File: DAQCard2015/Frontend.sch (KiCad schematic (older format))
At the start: 12 parts, among them U1 RJ45x8, U2 AD5628

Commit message: Various updates to DAQ board focusing on power system
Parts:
- P7: renamed from P?; footprint (none) -> extras:N3432-D302RB
- U2: footprint Housings_SSOP:TSSOP-16_4.4x5mm_Pitch0.65mm -> extras:TSSOP-16_4.4x5mm_Pitch0.65mm
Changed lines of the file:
@@
 F 0 "U2" H 20750 4250 60  0000 C CNN
 F 1 "AD5628" H 20250 5350 60  0000 C CNN
-F 2 "Housings_SSOP:TSSOP-16_4.4x5mm_Pitch0.65mm" H 20650 4950 60  0001 C CNN
+F 2 "extras:TSSOP-16_4.4x5mm_Pitch0.65mm" H 20650 4950 60  0001 C CNN
 F 3 "" H 20650 4950 60  0000 C CNN
 	1    20450 4800
@@
 	19750 4450 19900 4450
 Wire Wire Line
-	19750 4150 19750 4200
-Wire Wire Line
-	19750 4200 19750 4450
+	19750 4150 19750 4450
 Wire Wire Line
 	21000 4650 21500 4650
 Wire Wire Line
-	21500 5500 21500 5150
-Wire Wire Line
-	21500 5150 21500 4650
-Wire Wire Line
-	21500 4650 21500 4200
+	21500 5500 21500 4200
 Wire Wire Line
 	21500 4200 19750 4200
@@
 RNGDAC_CSB
 Wire Wire Line
-	19400 4650 19450 4650
-Wire Wire Line
-	19450 4650 19900 4650
+	19400 4650 19900 4650
 Text GLabel 19400 4650 0    60   Input ~ 0
 3V3dig
@@
 $EndComp
 Wire Wire Line
-	20300 5500 20400 5500
-Wire Wire Line
-	20400 5500 21500 5500
+	20300 5500 21500 5500
 Connection ~ 21500 5150
 $Comp
@@
 $EndComp
 Wire Wire Line
-	19800 5500 19900 5500
-Wire Wire Line
-	19900 5500 20000 5500
-Wire Wire Line
-	19900 5150 19900 5500
-Wire Wire Line
-	19900 5500 19900 5700
+	19800 5500 20000 5500
+Wire Wire Line
+	19900 5150 19900 5700
 Connection ~ 19900 5500
 Wire Wire Line
@@
 $EndComp
 Wire Wire Line
-	1250 4250 1450 4250
-Wire Wire Line
-	1450 4250 1750 4250
-Wire Wire Line
-	1750 4250 2000 4250
-Wire Wire Line
-	2000 4250 2400 4250
+	1250 4250 2400 4250
 Connection ~ 2000 4250
 Wire Wire Line
@@
 	1750 4250 1750 4200
 Wire Wire Line
-	1750 3800 1750 3850
-Wire Wire Line
-	1750 3850 1750 3900
+	1750 3800 1750 3900
 Wire Wire Line
 	2000 4250 2000 4200
@@
 	2000 3900 2000 3850
 Wire Wire Line
-	1750 3850 2000 3850
-Wire Wire Line
-	2000 3850 2400 3850
+	1750 3850 2400 3850
 Connection ~ 1750 3850
 Connection ~ 2000 3850
 Wire Wire Line
-	1250 3500 1450 3500
-Wire Wire Line
-	1450 3500 1750 3500
-Wire Wire Line
-	1750 3500 2400 3500
+	1250 3500 2400 3500
 Wire Wire Line
 	1450 3500 1450 3750
@@
 SDA
 Wire Wire Line
-	7700 11950 7950 11950
-Wire Wire Line
-	7950 11950 8250 11950
-Wire Wire Line
-	7700 12150 7950 12150
-Wire Wire Line
-	7950 12150 8250 12150
+	7700 11950 8250 11950
+Wire Wire Line
+	7700 12150 8250 12150
 Text Label 7700 12050 0    60   ~ 0
 SCL
@@
 SCL
 $Comp
-L CONN_02X20_Double P?
+L CONN_02X20_Double P7
 U 1 1 55F4BDE8
 P 7450 11200
-F 0 "P?" H 7950 12500 50  0000 C CNN
+F 0 "P7" H 7950 12500 50  0000 C CNN
 F 1 "CONN_02X20_Double" H 7950 12400 50  0000 C CNN
-F 2 "" H 7450 10250 60  0000 C CNN
+F 2 "extras:N3432-D302RB" H 7450 10250 60  0001 C CNN
 F 3 "" H 7450 10250 60  0000 C CNN
 	1    7450 11200
@@
 $EndComp
 Wire Wire Line
-	7950 11950 7950 12150
-Wire Wire Line
-	7950 12150 7950 12300
+	7950 11950 7950 12300
 Connection ~ 7950 11950
 Connection ~ 7950 12150
 Wire Wire Line
-	6900 12300 7950 12300
-Wire Wire Line
-	7950 12300 9000 12300
-Wire Wire Line
-	9000 12300 9000 12150
-Wire Wire Line
-	9000 12150 9000 11950
+	6900 12300 9000 12300
+Wire Wire Line
+	9000 12300 9000 11950
 Connection ~ 9000 12150
 Wire Wire Line
-	6900 11950 6900 12150
-Wire Wire Line
-	6900 12150 6900 12300
+	6900 11950 6900 12300
 Connection ~ 7950 12300
 Connection ~ 6900 12150

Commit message: Updates to DAQ Board focusing on the power system and flood fills for it
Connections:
- net GNDdig is gone; now on net GND: C4.2, R5.1, U2.1 (LDAC_N), U2.14 (GND), U2.9 (CLR_N)
- net ADC_CLK+: now also R3.1; no longer R3.2
- net ADC_CLK-: now also R3.2; no longer R3.1
- net 1ADC_Vref renamed ADC1_Vref
- net 2ADC_Vref renamed ADC2_Vref
- net 3ADC_Vref renamed ADC3_Vref
- net 4ADC_Vref renamed ADC4_Vref
- net 5ADC_Vref renamed ADC5_Vref
- net 6ADC_Vref renamed ADC6_Vref
- net 7ADC_Vref renamed ADC7_Vref
- net 8ADC_Vref renamed ADC8_Vref
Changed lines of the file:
@@
 $Descr A2 23386 16535
 encoding utf-8
-Sheet 2 13
+Sheet 5 13
 Title ""
 Date ""
@@
 F28 "Vocm" I T 4000 3250 60
 $EndSheet
-Text HLabel 5450 3250 1    60   Input ~ 0
-ADC_CLK+
-Text HLabel 5350 3250 1    60   Input ~ 0
-ADC_CLK-
 $Sheet
 S 14550 3250 3400 1050
@@
 Text HLabel 12650 4600 3    60   Output ~ 0
 3DCO+
-Text HLabel 4900 3250 1    60   Input ~ 0
-ADC_SCLK
-Text HLabel 5000 3250 1    60   Input ~ 0
-ADC_SDIO
-Text HLabel 5100 3250 1    60   Input ~ 0
-1ADC_CSB
 $Sheet
 S 7350 7050 3400 1050
@@
 Text HLabel 17600 4600 3    60   Output ~ 0
 4D-D
-Text HLabel 8700 3250 1    60   Input ~ 0
-2ADC_CSB
-Text HLabel 12300 3250 1    60   Input ~ 0
-3ADC_CSB
-Text HLabel 15900 3250 1    60   Input ~ 0
-4ADC_CSB
-Text HLabel 15900 7050 1    60   Input ~ 0
-5ADC_CSB
-Text HLabel 12300 7050 1    60   Input ~ 0
-6ADC_CSB
-Text HLabel 8700 7050 1    60   Input ~ 0
-7ADC_CSB
-Text HLabel 5100 7050 1    60   Input ~ 0
-8ADC_CSB
 $Comp
 L AD5628 U2
@@
 $EndComp
 Text GLabel 19750 4150 1    60   Input ~ 0
-GNDdig
+GND
 Wire Wire Line
 	19900 4550 19550 4550
@@
 	21500 4200 19750 4200
 Connection ~ 19750 4200
-Text HLabel 19550 4550 1    60   Input ~ 0
-RNGDAC_CSB
 Wire Wire Line
 	19400 4650 19900 4650
@@
 	4550 3250 4550 3100
 Text Label 4550 3100 2    60   ~ 0
-1ADC_Vref
+ADC1_Vref
 Wire Wire Line
 	8200 3250 8200 3100
 Text Label 8200 3100 2    60   ~ 0
-2ADC_Vref
+ADC2_Vref
 Wire Wire Line
 	11800 3250 11800 3100
 Text Label 11800 3100 2    60   ~ 0
-3ADC_Vref
+ADC3_Vref
 Wire Wire Line
 	15400 3250 15400 3100
 Text Label 15400 3100 2    60   ~ 0
-4ADC_Vref
+ADC4_Vref
 Wire Wire Line
 	15400 7050 15400 6900
 Text Label 15400 6900 2    60   ~ 0
-5ADC_Vref
+ADC5_Vref
 Wire Wire Line
 	11800 7050 11800 6900
 Text Label 11800 6900 2    60   ~ 0
-6ADC_Vref
+ADC6_Vref
 Wire Wire Line
 	8200 7050 8200 6900
 Text Label 8200 6900 2    60   ~ 0
-7ADC_Vref
+ADC7_Vref
 Wire Wire Line
 	4550 7050 4550 6900
 Text Label 4550 6900 2    60   ~ 0
-8ADC_Vref
+ADC8_Vref
 Text Label 19900 4850 2    60   ~ 0
-3ADC_Vref
+ADC3_Vref
 Text Label 19900 4750 2    60   ~ 0
-1ADC_Vref
+ADC1_Vref
 Text Label 21000 4750 0    60   ~ 0
-2ADC_Vref
+ADC2_Vref
 Text Label 21000 4850 0    60   ~ 0
-4ADC_Vref
+ADC4_Vref
 Text Label 21000 4950 0    60   ~ 0
-6ADC_Vref
+ADC6_Vref
 Text Label 21000 5050 0    60   ~ 0
-8ADC_Vref
+ADC8_Vref
 Text Label 19900 4950 2    60   ~ 0
-5ADC_Vref
+ADC5_Vref
 Text Label 19900 5050 2    60   ~ 0
-7ADC_Vref
+ADC7_Vref
 Wire Wire Line
 	21500 5150 21000 5150
@@
 F28 "Vocm" I T 7600 3250 60
 $EndSheet
-Text HLabel 8500 3250 1    60   Input ~ 0
-ADC_SCLK
-Text HLabel 12100 3250 1    60   Input ~ 0
-ADC_SCLK
-Text HLabel 15700 3250 1    60   Input ~ 0
-ADC_SCLK
-Text HLabel 15700 7050 1    60   Input ~ 0
-ADC_SCLK
-Text HLabel 12100 7050 1    60   Input ~ 0
-ADC_SCLK
-Text HLabel 8500 7050 1    60   Input ~ 0
-ADC_SCLK
-Text HLabel 4900 7050 1    60   Input ~ 0
-ADC_SCLK
-Text HLabel 8600 3250 1    60   Input ~ 0
-ADC_SDIO
-Text HLabel 12200 3250 1    60   Input ~ 0
-ADC_SDIO
-Text HLabel 15800 3250 1    60   Input ~ 0
-ADC_SDIO
 Text HLabel 21000 4550 2    60   Input ~ 0
 ADC_SDIO
 Text HLabel 21000 4450 2    60   Input ~ 0
 ADC_SCLK
-Text HLabel 15800 7050 1    60   Input ~ 0
-ADC_SDIO
-Text HLabel 12200 7050 1    60   Input ~ 0
-ADC_SDIO
-Text HLabel 8600 7050 1    60   Input ~ 0
-ADC_SDIO
-Text HLabel 5000 7050 1    60   Input ~ 0
-ADC_SDIO
-Text HLabel 9050 3250 1    60   Input ~ 0
-ADC_CLK+
-Text HLabel 8950 3250 1    60   Input ~ 0
-ADC_CLK-
-Text HLabel 12650 3250 1    60   Input ~ 0
-ADC_CLK+
-Text HLabel 12550 3250 1    60   Input ~ 0
-ADC_CLK-
-Text HLabel 16250 3250 1    60   Input ~ 0
-ADC_CLK+
-Text HLabel 16150 3250 1    60   Input ~ 0
-ADC_CLK-
-Text HLabel 16250 7050 1    60   Input ~ 0
-ADC_CLK+
-Text HLabel 16150 7050 1    60   Input ~ 0
-ADC_CLK-
-Text HLabel 12650 7050 1    60   Input ~ 0
-ADC_CLK+
-Text HLabel 12550 7050 1    60   Input ~ 0
-ADC_CLK-
-Text HLabel 9050 7050 1    60   Input ~ 0
-ADC_CLK+
-Text HLabel 8950 7050 1    60   Input ~ 0
-ADC_CLK-
-Text HLabel 5450 7050 1    60   Input ~ 0
-ADC_CLK+
-Text HLabel 5350 7050 1    60   Input ~ 0
-ADC_CLK-
-Text HLabel 3100 7700 1    60   Input ~ 0
-ADC_CLK-
-Text HLabel 3200 7700 1    60   Input ~ 0
-ADC_CLK+
 $Sheet
 S 3750 7050 3400 1050
@@
 Connection ~ 7950 12300
 Connection ~ 6900 12150
+Text GLabel 5450 3250 1    40   Input ~ 0
+ADC_CLK+
+Text GLabel 5350 3250 1    40   Input ~ 0
+ADC_CLK-
+Text GLabel 5100 3250 1    40   Input ~ 0
+ADC1_CSB
+Text GLabel 5000 3250 1    40   Input ~ 0
+SPI_SDIO
+Text GLabel 4900 3250 1    40   Input ~ 0
+SPI_SCLK
+Text GLabel 9050 3250 1    40   Input ~ 0
+ADC_CLK+
+Text GLabel 8950 3250 1    40   Input ~ 0
+ADC_CLK-
+Text GLabel 8700 3250 1    40   Input ~ 0
+ADC2_CSB
+Text GLabel 8600 3250 1    40   Input ~ 0
+SPI_SDIO
+Text GLabel 8500 3250 1    40   Input ~ 0
+SPI_SCLK
+Text GLabel 12650 3250 1    40   Input ~ 0
+ADC_CLK+
+Text GLabel 12550 3250 1    40   Input ~ 0
+ADC_CLK-
+Text GLabel 12300 3250 1    40   Input ~ 0
+ADC3_CSB
+Text GLabel 12200 3250 1    40   Input ~ 0
+SPI_SDIO
+Text GLabel 12100 3250 1    40   Input ~ 0
+SPI_SCLK
+Text GLabel 16250 3250 1    40   Input ~ 0
+ADC_CLK+
+Text GLabel 16150 3250 1    40   Input ~ 0
+ADC_CLK-
+Text GLabel 15900 3250 1    40   Input ~ 0
+ADC4_CSB
+Text GLabel 15800 3250 1    40   Input ~ 0
+SPI_SDIO
+Text GLabel 15700 3250 1    40   Input ~ 0
+SPI_SCLK
+Text GLabel 16250 7050 1    40   Input ~ 0
+ADC_CLK+
+Text GLabel 16150 7050 1    40   Input ~ 0
+ADC_CLK-
+Text GLabel 15900 7050 1    40   Input ~ 0
+ADC5_CSB
+Text GLabel 15800 7050 1    40   Input ~ 0
+SPI_SDIO
+Text GLabel 15700 7050 1    40   Input ~ 0
+SPI_SCLK
+Text GLabel 12650 7050 1    40   Input ~ 0
+ADC_CLK+
+Text GLabel 12550 7050 1    40   Input ~ 0
+ADC_CLK-
+Text GLabel 12300 7050 1    40   Input ~ 0
+ADC6_CSB
+Text GLabel 12200 7050 1    40   Input ~ 0
+SPI_SDIO
+Text GLabel 12100 7050 1    40   Input ~ 0
+SPI_SCLK
+Text GLabel 9050 7050 1    40   Input ~ 0
+ADC_CLK+
+Text GLabel 8950 7050 1    40   Input ~ 0
+ADC_CLK-
+Text GLabel 8700 7050 1    40   Input ~ 0
+ADC7_CSB
+Text GLabel 8600 7050 1    40   Input ~ 0
+SPI_SDIO
+Text GLabel 8500 7050 1    40   Input ~ 0
+SPI_SCLK
+Text GLabel 5450 7050 1    40   Input ~ 0
+ADC_CLK+
+Text GLabel 5350 7050 1    40   Input ~ 0
+ADC_CLK-
+Text GLabel 5100 7050 1    40   Input ~ 0
+ADC8_CSB
+Text GLabel 5000 7050 1    40   Input ~ 0
+SPI_SDIO
+Text GLabel 4900 7050 1    40   Input ~ 0
+SPI_SCLK
+Text GLabel 3100 7700 1    40   Input ~ 0
+ADC_CLK+
+Text GLabel 3200 7700 1    40   Input ~ 0
+ADC_CLK-
+Text GLabel 19550 4550 1    60   Input ~ 0
+RNGDAC_CSB
+Text GLabel 10250 10300 2    40   Input ~ 0
+Vana
+Text GLabel 10250 10400 2    40   Input ~ 0
+Vana
+Text GLabel 10250 10500 2    40   Input ~ 0
+Vana
+Text GLabel 10250 10600 2    40   Input ~ 0
+Vana
+Text GLabel 10250 10700 2    40   Input ~ 0
+Vana
+Text GLabel 10250 10800 2    40   Input ~ 0
+Vana
+Text GLabel 10250 10900 2    40   Input ~ 0
+Vana
+Text GLabel 10250 11000 2    40   Input ~ 0
+Vana
+Text GLabel 10250 11100 2    40   Input ~ 0
+Vana
+Text GLabel 10250 11200 2    40   Input ~ 0
+Vana
+Text GLabel 10250 11300 2    40   Input ~ 0
+Vana
+Text GLabel 10250 11400 2    40   Input ~ 0
+Vana
 $EndSCHEMATC

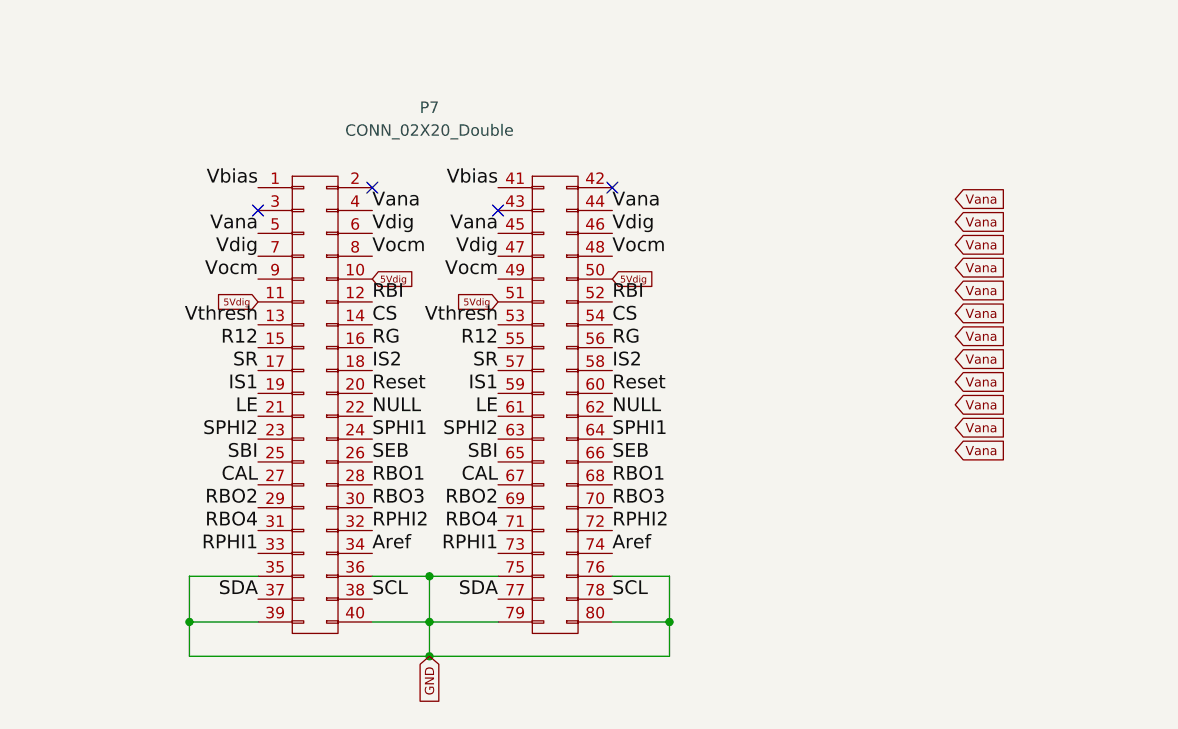
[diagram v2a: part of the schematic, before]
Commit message: Updates to DAQ board focusing on Support electronics
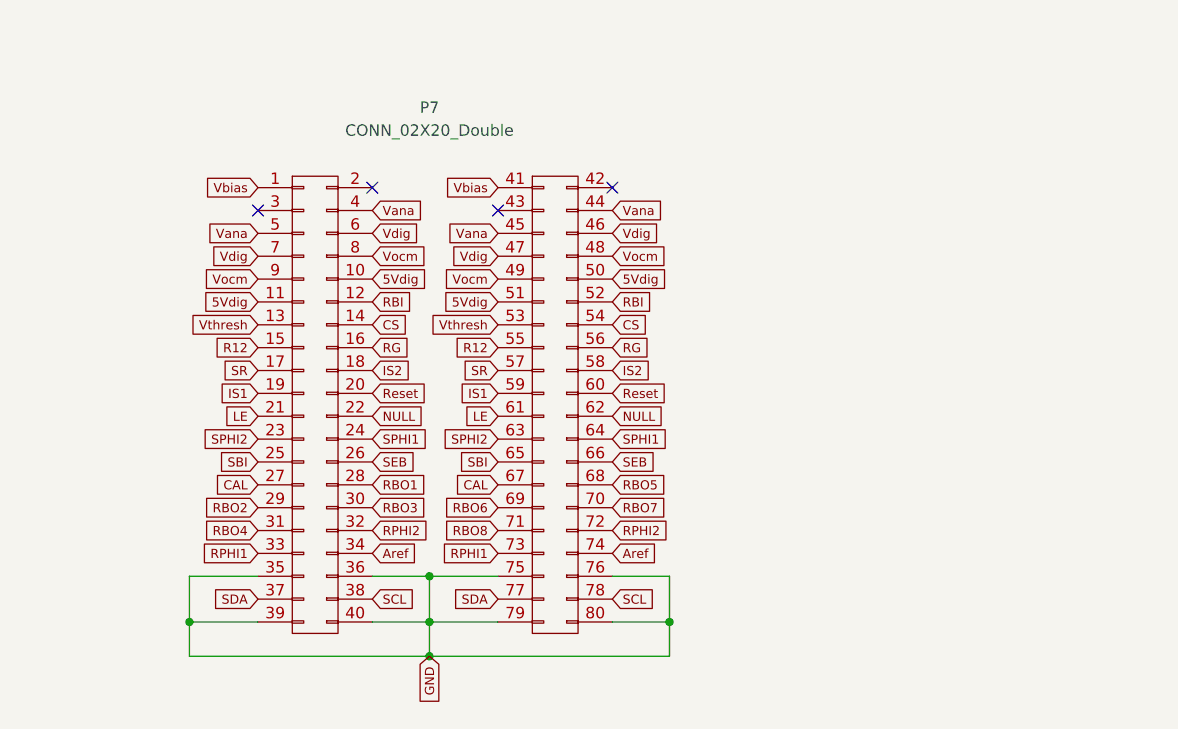
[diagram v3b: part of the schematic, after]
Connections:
- net RBO1: no longer P7.68 (P28)
- net RBO2: no longer P7.69 (P29)
- net RBO3: no longer P7.70 (P30)
- net RBO4: no longer P7.71 (P31)
- new net RBO5: P7.68 (P28)
- new net RBO6: P7.69 (P29)
- new net RBO7: P7.70 (P30)
- new net RBO8: P7.71 (P31)
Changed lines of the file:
@@
 Wire Wire Line
 	17350 2650 17350 2550
-Text Label 7200 10250 2    60   ~ 0
-Vbias
 NoConn ~ 7700 10250
 NoConn ~ 7200 10350
-Text Label 7700 10350 0    60   ~ 0
-Vana
-Text Label 7200 10450 2    60   ~ 0
-Vana
-Text Label 7700 10450 0    60   ~ 0
-Vdig
-Text Label 7200 10550 2    60   ~ 0
-Vdig
-Text Label 7700 10550 0    60   ~ 0
-Vocm
-Text Label 7200 10650 2    60   ~ 0
-Vocm
-Text GLabel 7700 10650 2    30   Input ~ 0
-5Vdig
-Text GLabel 7200 10750 0    30   Input ~ 0
-5Vdig
-Text Label 7700 10750 0    60   ~ 0
-RBI
-Wire Wire Line
-	7200 10750 7200 10750
-Wire Wire Line
-	7700 10650 7700 10650
-Text Label 7200 10850 2    60   ~ 0
-Vthresh
-Text Label 7700 10850 0    60   ~ 0
-CS
-Text Label 7200 10950 2    60   ~ 0
-R12
-Text Label 7700 10950 0    60   ~ 0
-RG
-Text Label 7200 11050 2    60   ~ 0
-SR
-Text Label 7700 11050 0    60   ~ 0
-IS2
-Text Label 7200 11150 2    60   ~ 0
-IS1
-Text Label 7700 11150 0    60   ~ 0
-Reset
-Text Label 7200 11250 2    60   ~ 0
-LE
-Text Label 7700 11250 0    60   ~ 0
-NULL
-Text Label 7200 11350 2    60   ~ 0
-SPHI2
-Text Label 7700 11350 0    60   ~ 0
-SPHI1
-Text Label 7200 11450 2    60   ~ 0
-SBI
-Text Label 7700 11450 0    60   ~ 0
-SEB
-Text Label 7200 11550 2    60   ~ 0
-CAL
-Text Label 7700 11550 0    60   ~ 0
-RBO1
-Text Label 7200 11650 2    60   ~ 0
-RBO2
-Text Label 7700 11650 0    60   ~ 0
-RBO3
-Text Label 7200 11750 2    60   ~ 0
-RBO4
-Text Label 7700 11750 0    60   ~ 0
-RPHI2
-Text Label 7200 11850 2    60   ~ 0
-RPHI1
-Text Label 7700 11850 0    60   ~ 0
-Aref
 Wire Wire Line
 	6900 11950 7200 11950
 Wire Wire Line
 	6900 12150 7200 12150
-Text Label 7200 12050 2    60   ~ 0
-SDA
 Wire Wire Line
 	7700 11950 8250 11950
 Wire Wire Line
 	7700 12150 8250 12150
-Text Label 7700 12050 0    60   ~ 0
-SCL
-Text Label 8250 10250 2    60   ~ 0
-Vbias
 NoConn ~ 8750 10250
 NoConn ~ 8250 10350
-Text Label 8750 10350 0    60   ~ 0
-Vana
-Text Label 8250 10450 2    60   ~ 0
-Vana
-Text Label 8750 10450 0    60   ~ 0
-Vdig
-Text Label 8250 10550 2    60   ~ 0
-Vdig
-Text Label 8750 10550 0    60   ~ 0
-Vocm
-Text Label 8250 10650 2    60   ~ 0
-Vocm
-Text GLabel 8750 10650 2    30   Input ~ 0
-5Vdig
-Text GLabel 8250 10750 0    30   Input ~ 0
-5Vdig
-Text Label 8750 10750 0    60   ~ 0
-RBI
-Wire Wire Line
-	8250 10750 8250 10750
-Wire Wire Line
-	8750 10650 8750 10650
-Text Label 8250 10850 2    60   ~ 0
-Vthresh
-Text Label 8750 10850 0    60   ~ 0
-CS
-Text Label 8250 10950 2    60   ~ 0
-R12
-Text Label 8750 10950 0    60   ~ 0
-RG
-Text Label 8250 11050 2    60   ~ 0
-SR
-Text Label 8750 11050 0    60   ~ 0
-IS2
-Text Label 8250 11150 2    60   ~ 0
-IS1
-Text Label 8750 11150 0    60   ~ 0
-Reset
-Text Label 8250 11250 2    60   ~ 0
-LE
-Text Label 8750 11250 0    60   ~ 0
-NULL
-Text Label 8250 11350 2    60   ~ 0
-SPHI2
-Text Label 8750 11350 0    60   ~ 0
-SPHI1
-Text Label 8250 11450 2    60   ~ 0
-SBI
-Text Label 8750 11450 0    60   ~ 0
-SEB
-Text Label 8250 11550 2    60   ~ 0
-CAL
-Text Label 8750 11550 0    60   ~ 0
-RBO1
-Text Label 8250 11650 2    60   ~ 0
-RBO2
-Text Label 8750 11650 0    60   ~ 0
-RBO3
-Text Label 8250 11750 2    60   ~ 0
-RBO4
-Text Label 8750 11750 0    60   ~ 0
-RPHI2
-Text Label 8250 11850 2    60   ~ 0
-RPHI1
-Text Label 8750 11850 0    60   ~ 0
-Aref
 Text GLabel 7950 12300 3    40   Input ~ 0
 GND
-Text Label 8250 12050 2    60   ~ 0
-SDA
 Wire Wire Line
 	8750 11950 9000 11950
 Wire Wire Line
 	8750 12150 9000 12150
-Text Label 8750 12050 0    60   ~ 0
-SCL
 $Comp
 L CONN_02X20_Double P7
@@
 Text GLabel 19550 4550 1    60   Input ~ 0
 RNGDAC_CSB
-Text GLabel 10250 10300 2    40   Input ~ 0
-Vana
-Text GLabel 10250 10400 2    40   Input ~ 0
-Vana
-Text GLabel 10250 10500 2    40   Input ~ 0
-Vana
-Text GLabel 10250 10600 2    40   Input ~ 0
-Vana
-Text GLabel 10250 10700 2    40   Input ~ 0
-Vana
-Text GLabel 10250 10800 2    40   Input ~ 0
-Vana
-Text GLabel 10250 10900 2    40   Input ~ 0
-Vana
-Text GLabel 10250 11000 2    40   Input ~ 0
-Vana
-Text GLabel 10250 11100 2    40   Input ~ 0
-Vana
-Text GLabel 10250 11200 2    40   Input ~ 0
-Vana
-Text GLabel 10250 11300 2    40   Input ~ 0
-Vana
-Text GLabel 10250 11400 2    40   Input ~ 0
-Vana
+Text GLabel 7700 10350 2    40   Input ~ 0
+Vana
+Text GLabel 7700 10450 2    40   Input ~ 0
+Vdig
+Text GLabel 7700 10550 2    40   Input ~ 0
+Vocm
+Text GLabel 7700 10750 2    40   Input ~ 0
+RBI
+Text GLabel 7700 10850 2    40   Input ~ 0
+CS
+Text GLabel 7700 10950 2    40   Input ~ 0
+RG
+Text GLabel 7700 11050 2    40   Input ~ 0
+IS2
+Text GLabel 7700 11150 2    40   Input ~ 0
+Reset
+Text GLabel 7700 11250 2    40   Input ~ 0
+NULL
+Text GLabel 7700 11350 2    40   Input ~ 0
+SPHI1
+Text GLabel 7700 11450 2    40   Input ~ 0
+SEB
+Text GLabel 7700 11550 2    40   Input ~ 0
+RBO1
+Text GLabel 7700 11650 2    40   Input ~ 0
+RBO3
+Text GLabel 7700 11750 2    40   Input ~ 0
+RPHI2
+Text GLabel 7700 11850 2    40   Input ~ 0
+Aref
+Text GLabel 7700 10650 2    40   Input ~ 0
+5Vdig
+Text GLabel 7200 11850 0    40   Input ~ 0
+RPHI1
+Text GLabel 7200 11750 0    40   Input ~ 0
+RBO4
+Text GLabel 7200 11650 0    40   Input ~ 0
+RBO2
+Text GLabel 7200 11450 0    40   Input ~ 0
+SBI
+Text GLabel 7200 11350 0    40   Input ~ 0
+SPHI2
+Text GLabel 7200 11250 0    40   Input ~ 0
+LE
+Text GLabel 7200 11150 0    40   Input ~ 0
+IS1
+Text GLabel 7200 11050 0    40   Input ~ 0
+SR
+Text GLabel 7200 10950 0    40   Input ~ 0
+R12
+Text GLabel 7200 10850 0    40   Input ~ 0
+Vthresh
+Text GLabel 7200 10750 0    40   Input ~ 0
+5Vdig
+Text GLabel 7200 10650 0    40   Input ~ 0
+Vocm
+Text GLabel 7200 10550 0    40   Input ~ 0
+Vdig
+Text GLabel 7200 10450 0    40   Input ~ 0
+Vana
+Text GLabel 7200 10250 0    40   Input ~ 0
+Vbias
+Text GLabel 7200 11550 0    40   Input ~ 0
+CAL
+Text GLabel 7200 12050 0    40   Input ~ 0
+SDA
+Text GLabel 7700 12050 2    40   Input ~ 0
+SCL
+Text GLabel 8250 11850 0    40   Input ~ 0
+RPHI1
+Text GLabel 8250 11750 0    40   Input ~ 0
+RBO8
+Text GLabel 8250 11650 0    40   Input ~ 0
+RBO6
+Text GLabel 8250 11450 0    40   Input ~ 0
+SBI
+Text GLabel 8250 11350 0    40   Input ~ 0
+SPHI2
+Text GLabel 8250 11250 0    40   Input ~ 0
+LE
+Text GLabel 8250 11150 0    40   Input ~ 0
+IS1
+Text GLabel 8250 11050 0    40   Input ~ 0
+SR
+Text GLabel 8250 10950 0    40   Input ~ 0
+R12
+Text GLabel 8250 10850 0    40   Input ~ 0
+Vthresh
+Text GLabel 8250 10750 0    40   Input ~ 0
+5Vdig
+Text GLabel 8250 10650 0    40   Input ~ 0
+Vocm
+Text GLabel 8250 10550 0    40   Input ~ 0
+Vdig
+Text GLabel 8250 10450 0    40   Input ~ 0
+Vana
+Text GLabel 8250 10250 0    40   Input ~ 0
+Vbias
+Text GLabel 8250 11550 0    40   Input ~ 0
+CAL
+Text GLabel 8250 12050 0    40   Input ~ 0
+SDA
+Text GLabel 8750 10350 2    40   Input ~ 0
+Vana
+Text GLabel 8750 10450 2    40   Input ~ 0
+Vdig
+Text GLabel 8750 10550 2    40   Input ~ 0
+Vocm
+Text GLabel 8750 10750 2    40   Input ~ 0
+RBI
+Text GLabel 8750 10850 2    40   Input ~ 0
+CS
+Text GLabel 8750 10950 2    40   Input ~ 0
+RG
+Text GLabel 8750 11050 2    40   Input ~ 0
+IS2
+Text GLabel 8750 11150 2    40   Input ~ 0
+Reset
+Text GLabel 8750 11250 2    40   Input ~ 0
+NULL
+Text GLabel 8750 11350 2    40   Input ~ 0
+SPHI1
+Text GLabel 8750 11450 2    40   Input ~ 0
+SEB
+Text GLabel 8750 11550 2    40   Input ~ 0
+RBO5
+Text GLabel 8750 11650 2    40   Input ~ 0
+RBO7
+Text GLabel 8750 11750 2    40   Input ~ 0
+RPHI2
+Text GLabel 8750 11850 2    40   Input ~ 0
+Aref
+Text GLabel 8750 10650 2    40   Input ~ 0
+5Vdig
+Text GLabel 8750 12050 2    40   Input ~ 0
+SCL
 $EndSCHEMATC
